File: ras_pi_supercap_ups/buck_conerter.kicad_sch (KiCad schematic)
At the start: 18 parts, among them U10 TPS54331DR

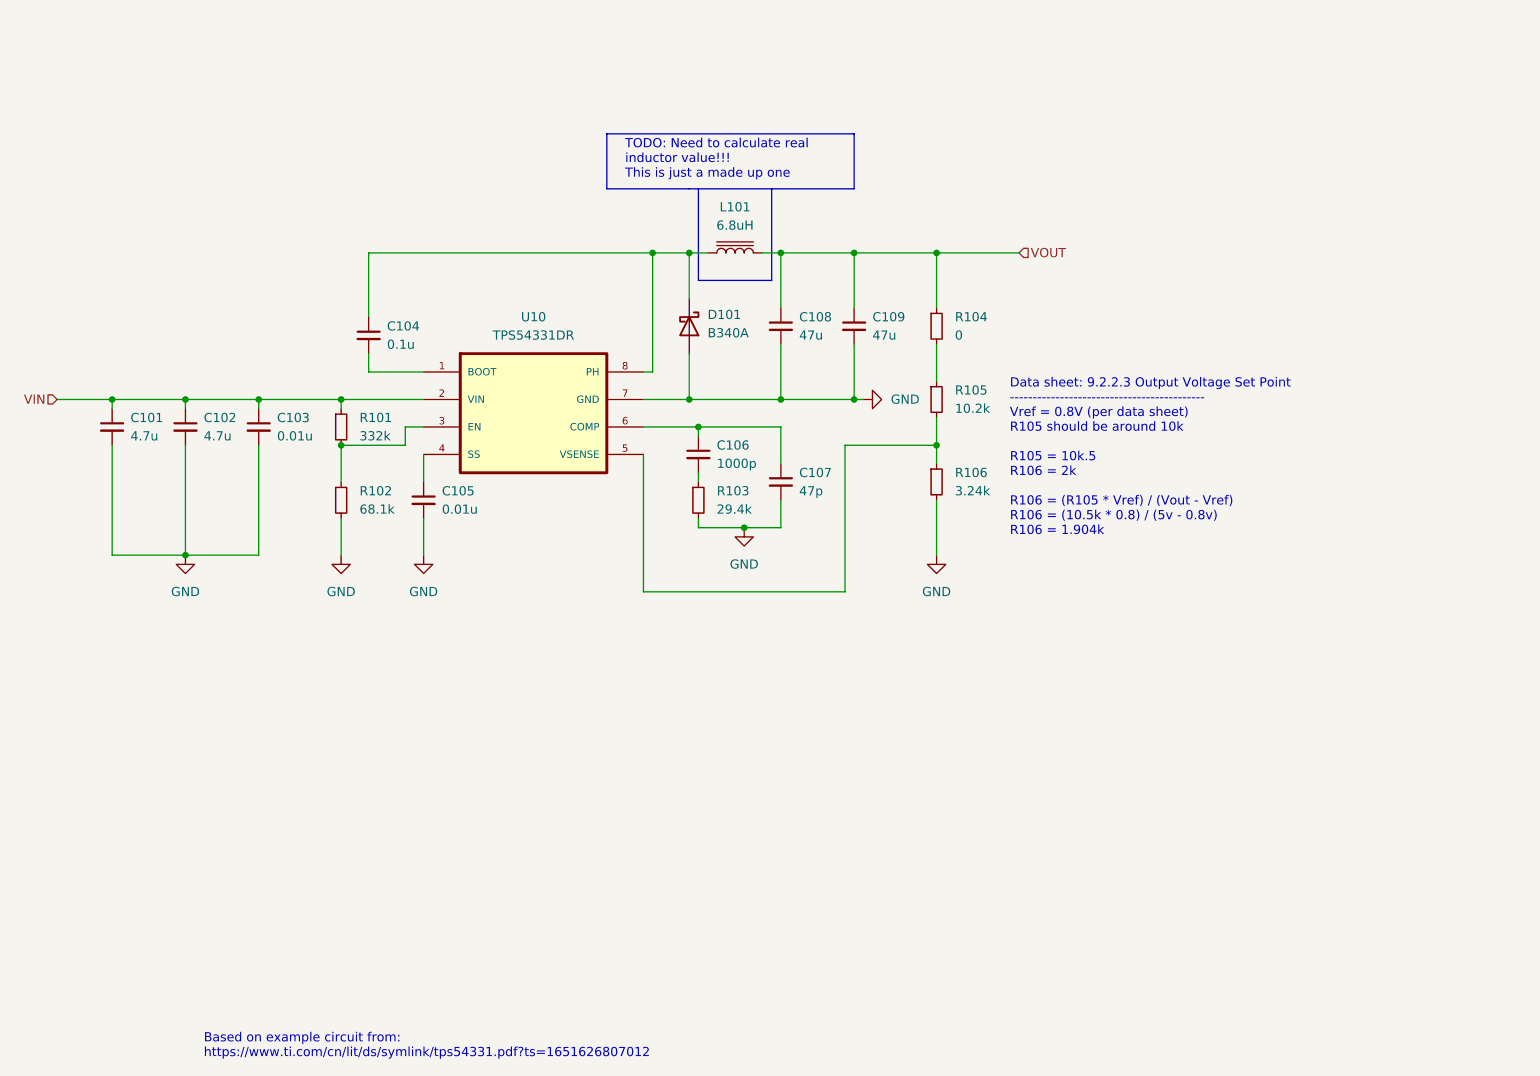
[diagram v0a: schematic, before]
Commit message: added 3d model
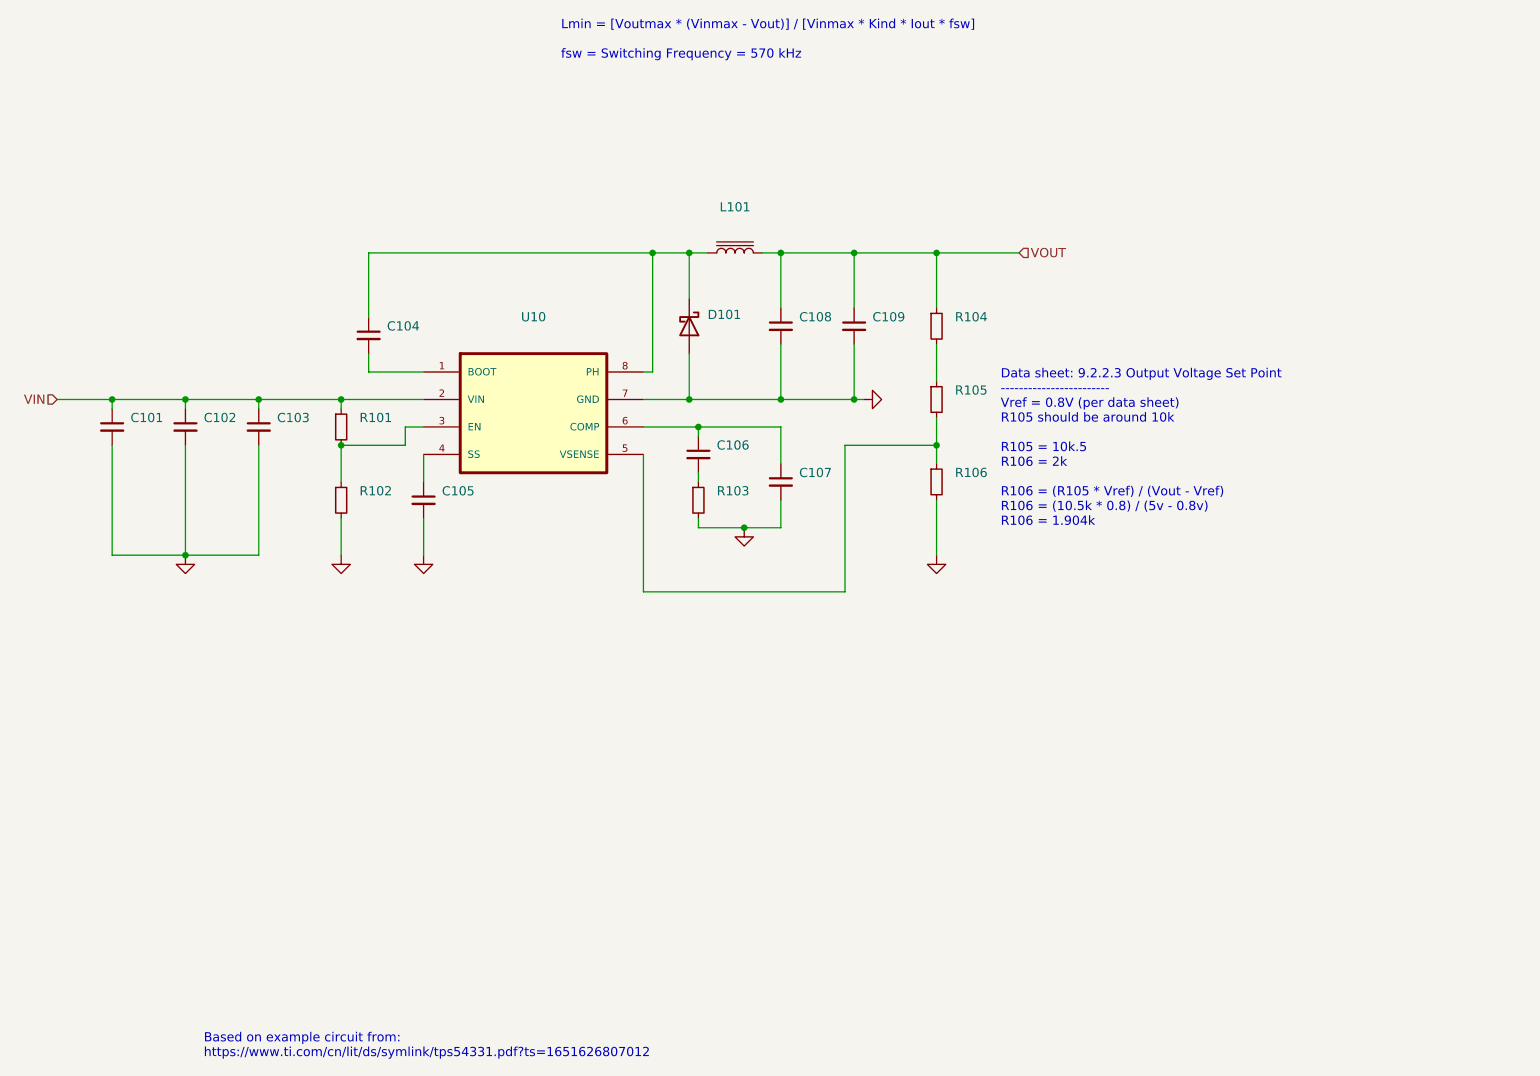
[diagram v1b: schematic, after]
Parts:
- C101, C102: value 4.7u -> ~; footprint Capacitor_SMD:C_0805_2012Metric -> (none); LCSC (none) -> C1779
- C103: value 0.01u -> ~; footprint Capacitor_SMD:C_0805_2012Metric -> (none); LCSC (none) -> C1744
- C104: value 0.1u -> ~; footprint Capacitor_SMD:C_0805_2012Metric -> (none); LCSC (none) -> C28233
- C105: value 0.01u -> ~; footprint Capacitor_SMD:C_0805_2012Metric -> (none); LCSC (none) -> C1710
- C106: value 1000p -> ~; footprint Capacitor_SMD:C_0805_2012Metric -> (none); LCSC (none) -> C1744
- C107: value 47p -> ~; footprint Capacitor_SMD:C_0805_2012Metric -> (none)
- C108, C109: value 47u -> ~; footprint Capacitor_SMD:C_0805_2012Metric -> (none); LCSC (none) -> C342635
- D101: value B340A -> ~; footprint Diode_SMD:D_SMA -> (none)
- L101: value 6.8uH -> ~; footprint Inductor_SMD:L_6.3x6.3_H3 -> (none); LCSC (none) -> C325965
- R101: value 332k -> ~; footprint Resistor_SMD:R_0805_2012Metric -> (none)
- R102: value 68.1k -> ~; footprint Resistor_SMD:R_0805_2012Metric -> (none)
- R103: value 29.4k -> ~; footprint Resistor_SMD:R_0805_2012Metric -> (none)
- R104: value 0 -> ~; footprint Resistor_SMD:R_0805_2012Metric -> (none)
- R105: value 10.2k -> ~; footprint Resistor_SMD:R_0805_2012Metric -> (none)
- R106: value 3.24k -> ~; footprint Resistor_SMD:R_0805_2012Metric -> (none)
- U10: value TPS54331DR -> ~; footprint SOIC127P599X175-8N -> (none)
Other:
- note added: "Data sheet: 9.2.2.3 Output Voltage Set Point ------------------------ Vref = 0.8V (per data sheet) R105 should be around 10k R105 = 10k.5 R106 = 2k R106 = (R105 * Vref) / (Vout - Vref) R106 = (10.5k * 0.8) / (5v - 0.8v) R106 = 1.904k"
- note added: "Lmin = [Voutmax * (Vinmax - Vout)] / [Vinmax * Kind * Iout * fsw] fsw = Switching Frequency = 570 kHz"
- note removed: "Data sheet: 9.2.2.3 Output Voltage Set Point ------------------------------------------- Vref = 0.8V (per data sheet) R105 should be around 10k R105 = 10k.5 R106 = 2k R106 = (R105 * Vref) / (Vout - Vref) R106 = (10.5k * 0.8) / (5v - 0.8v) R106 = 1.904k"
- note removed: "TODO: Need to calculate real inductor value!!! This is just a made up one"

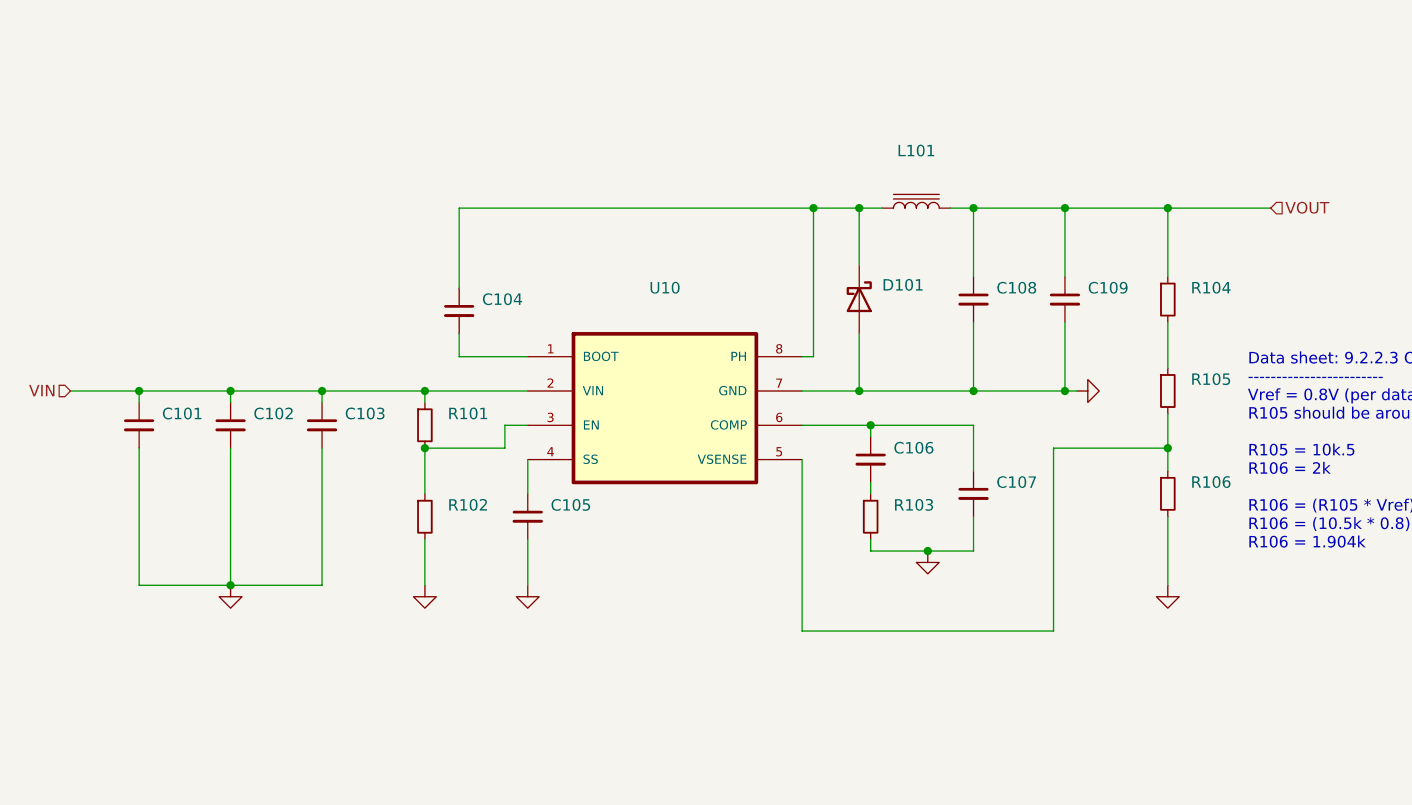
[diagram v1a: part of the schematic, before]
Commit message: updated layout
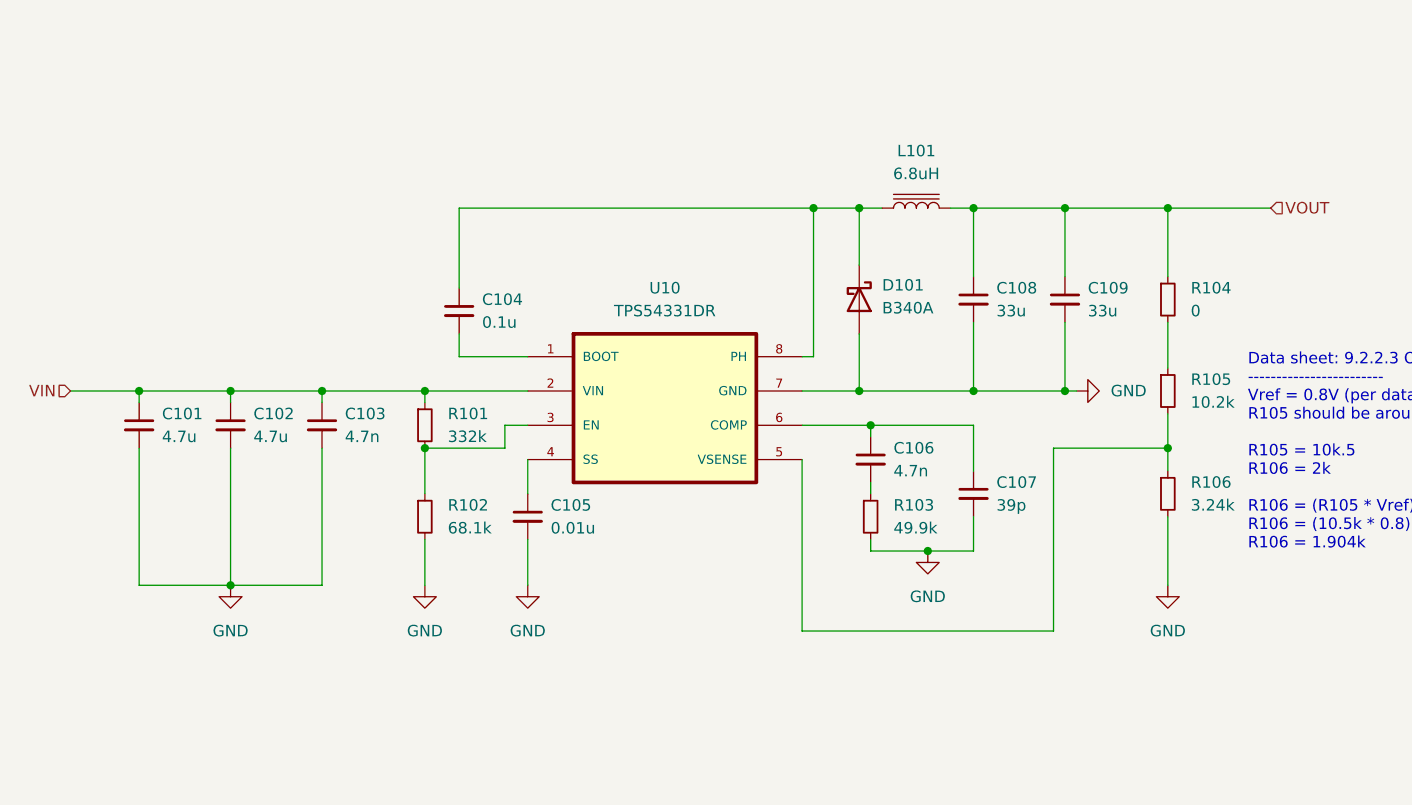
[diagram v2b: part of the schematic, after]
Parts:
- C101, C102: value ~ -> 4.7u; footprint (none) -> Capacitor_SMD:C_0805_2012Metric
- C103, C106: value ~ -> 4.7n; footprint (none) -> Capacitor_SMD:C_0805_2012Metric
- C104: value ~ -> 0.1u; footprint (none) -> Capacitor_SMD:C_0805_2012Metric
- C105: value ~ -> 0.01u; footprint (none) -> Capacitor_SMD:C_0805_2012Metric
- C107: value ~ -> 39p; footprint (none) -> Capacitor_SMD:C_0805_2012Metric
- C108, C109: value ~ -> 33u; footprint (none) -> Capacitor_SMD:C_0805_2012Metric
- D101: value ~ -> B340A; footprint (none) -> Diode_SMD:D_SMA
- L101: value ~ -> 6.8uH; footprint (none) -> raspberrypi_supercap_ups_lib:Sunltech_SLO0530H
- R101: value ~ -> 332k; footprint (none) -> Resistor_SMD:R_0805_2012Metric
- R102: value ~ -> 68.1k; footprint (none) -> Resistor_SMD:R_0805_2012Metric
- R103: value ~ -> 49.9k; footprint (none) -> Resistor_SMD:R_0805_2012Metric
- R104: value ~ -> 0; footprint (none) -> Resistor_SMD:R_0805_2012Metric
- R105: value ~ -> 10.2k; footprint (none) -> Resistor_SMD:R_0805_2012Metric
- R106: value ~ -> 3.24k; footprint (none) -> Resistor_SMD:R_0805_2012Metric
- U10: value ~ -> TPS54331DR; footprint (none) -> SOIC127P599X175-8N
